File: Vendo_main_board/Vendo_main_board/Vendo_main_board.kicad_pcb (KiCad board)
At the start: 2 copper layers, 60 x 100 mm, 98 parts, among them J1 Screw_Terminal_01x04, J10 Screw_Terminal_01x03, J11 Screw_Terminal_01x02, J12 Screw_Terminal_01x03, J2 Barrel_Jack_MountingPin, J3 Conn_01x05_Pin, J4 Conn_01x05_Pin, J5 BOOT, J6 Screw_Terminal_01x04, J7 FTDI, J9 Conn_01x04_Pin, Q1 Q_NMOS_Depletion_GSD, Q2 Q_NMOS_Depletion_GSD, Q3 Q_NMOS_Depletion_GSD, SW1 SW_Push, SW2 SW_Push, SW3 SW_Push, SW4 SW_Push, SW5 SW_Slide_DPDT, U1 AMS1117-3.3, U2 AP64350SP-13, U3 STM32F103C8T6, U4 PC817, Y1 32.768kHz, Y2 8MHz

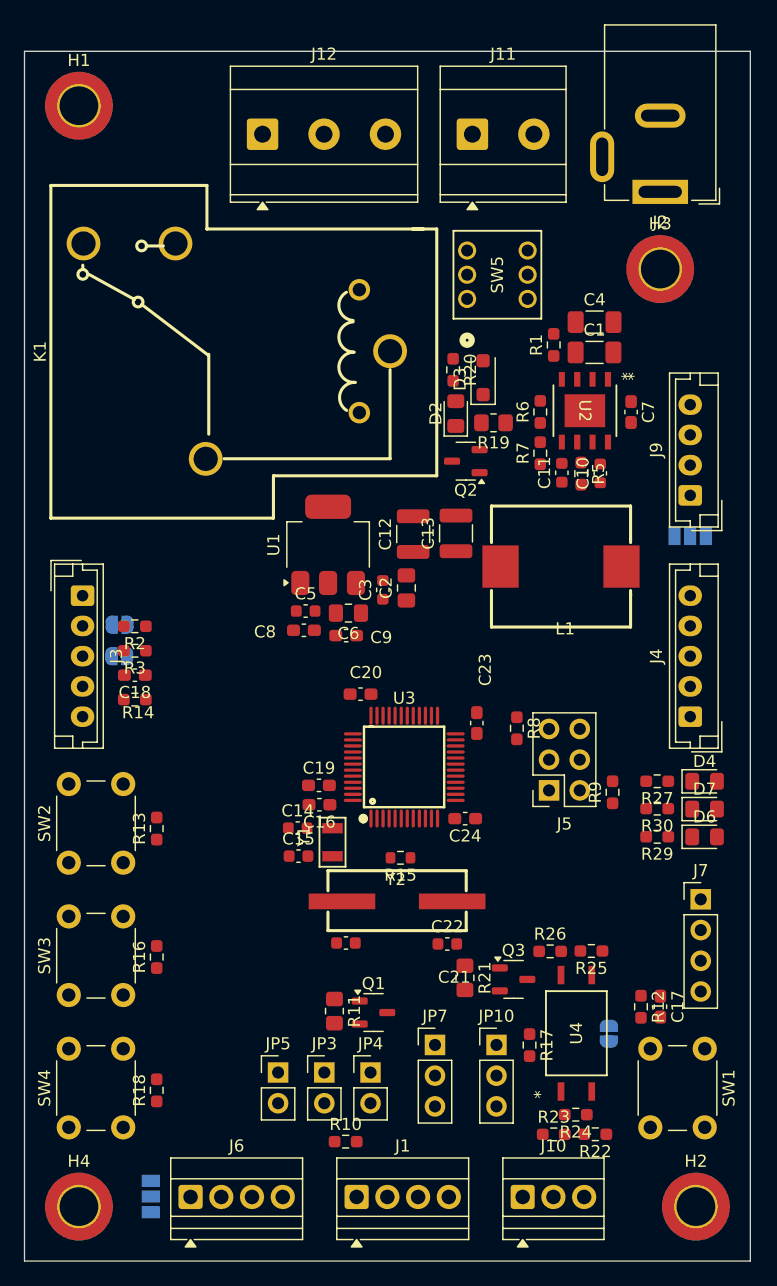
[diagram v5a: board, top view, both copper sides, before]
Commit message: -update schematic and placement
-added buzzer
-finalize pcb placement
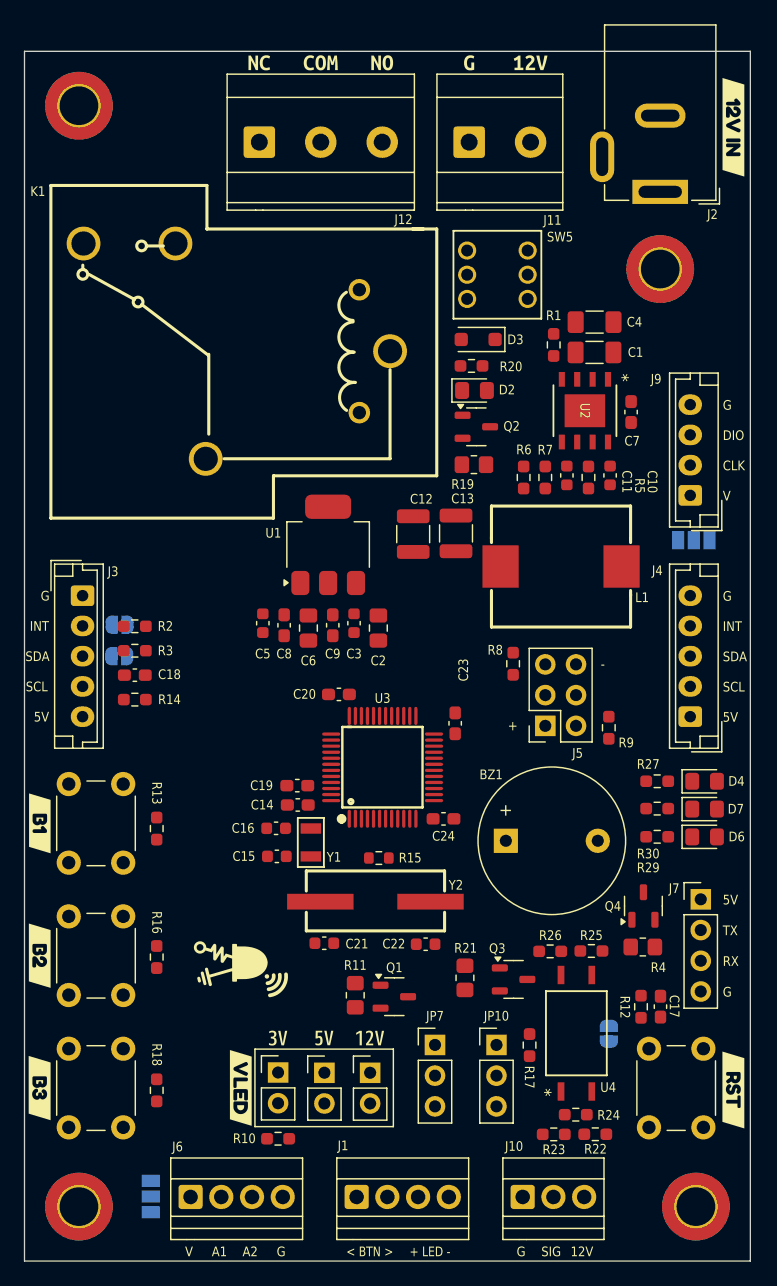
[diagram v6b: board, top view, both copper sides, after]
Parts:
- added BZ1: Buzzer, Buzzer_Beeper:Buzzer_12x9.5RM7.6, F.Cu at (237.9, 92.9)
- added G***: LOGO, InnovKits:innov_logo_5, F.Cu at (216.0, 103.4)
- added G***: LOGO, InnovKits:innov_logo_5, B.Cu at (228.6, 64.7)
- added Q4: Q_NMOS_Depletion_GSD, Package_TO_SOT_SMD:SOT-23-3, F.Cu at (249.3, 98.2)
- added R4: 10K, Resistor_SMD:R_0805_2012Metric_Pad1.20x1.40mm_HandSolder, F.Cu at (249.2, 101.6)
- added kibuzzard-6A0C4EC9: G***, kibuzzard-6A0C4EC9, F.Cu at (234.9, 28.6)
- added kibuzzard-6A0C4ED1: G***, kibuzzard-6A0C4ED1, F.Cu at (227.7, 28.6)
- added kibuzzard-6A0C4EDA: G***, kibuzzard-6A0C4EDA, F.Cu at (222.6, 28.6)
- added kibuzzard-6A0C4EE4: G***, kibuzzard-6A0C4EE4, F.Cu at (217.5, 28.6)
- added kibuzzard-6A0C4FB5: G***, kibuzzard-6A0C4FB5, F.Cu at (239.9, 28.5)
- added kibuzzard-6A0C5003: G***, kibuzzard-6A0C5003, F.Cu at (256.7, 33.9)
- added kibuzzard-6A0C536D: G***, kibuzzard-6A0C536D, F.Cu at (256.7, 113.5)
- added kibuzzard-6A0C57A3: G***, kibuzzard-6A0C57A3, F.Cu at (199.4, 91.4)
- added kibuzzard-6A0C57A8: G***, kibuzzard-6A0C57A8, F.Cu at (199.4, 102.4)
- added kibuzzard-6A0C57AC: G***, kibuzzard-6A0C57AC, F.Cu at (199.3, 113.3)
- added kibuzzard-6A0C5E83: G***, kibuzzard-6A0C5E83, F.Cu at (226.7, 109.2)
- added kibuzzard-6A0C5E89: G***, kibuzzard-6A0C5E89, F.Cu at (222.9, 109.2)
- added kibuzzard-6A0C5E92: G***, kibuzzard-6A0C5E92, F.Cu at (219.1, 109.2)
- added kibuzzard-6A0C5F1E: G***, kibuzzard-6A0C5F1E, F.Cu at (216.0, 113.3)
- moved R10 5.59 mm to (219.1, 117.5)
- moved R6 5.59 mm to (239.4, 62.8), turned to -90 degrees
- moved R8 5.34 mm to (238.5, 78.2)
- moved J5 5.34 mm to (241.2, 83.4)
- moved R9 5.34 mm to (246.4, 83.5)
- moved C2 4.05 mm to (227.3, 75.3)
- moved R19 3.82 mm to (235.2, 61.8)
- moved JP4 3.81 mm to (222.9, 112.0)
- moved JP3 3.79 mm to (226.7, 112.0)
- moved C5 3.68 mm to (217.8, 74.9), turned to 90 degrees
- moved C3 3.64 mm to (225.3, 74.9)
- moved C6 3.53 mm to (221.6, 75.3), turned to 90 degrees
- moved D3 3.18 mm to (235.6, 51.4), turned to 180 degrees
- moved Q2 2.97 mm to (235.4, 58.6), turned to 0 degrees
- moved D2 2.46 mm to (235.3, 55.6), turned to 0 degrees
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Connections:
- J3 pad 1: +5V -> GND
- J3 pad 2: STM_SCL -> I2C_INT
- J3 pad 4: I2C_INT -> STM_SCL
- J3 pad 5: GND -> +5V
- U3 pad 11: unconnected-(U3-PA1-Pad11) -> BUZZER
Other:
- board text added: "+"
- board text added: "+ LED -"
- board text added: "-"
- board text added: "12V"
- board text added: "5V"
- board text added: "< BTN >"
- board text added: "A1"
- board text added: "A2"
- board text added: "CLK"
- board text added: "DESIGNED AND MANUFACTURED BY:"
- board text added: "DIO"
- board text added: "DRIVING INNOVATION FOR LONG TERM SOLUTIONS"
- board text added: "G"
- board text added: "INNOVATION CENTRAL PH"
- board text added: "INT"
- board text added: "RX"
- board text added: "SCL"
- board text added: "SDA"
- board text added: "SIG"
- board text added: "TX"
- board text added: "V"
- board text added: "VENDO BOARD V1.0"

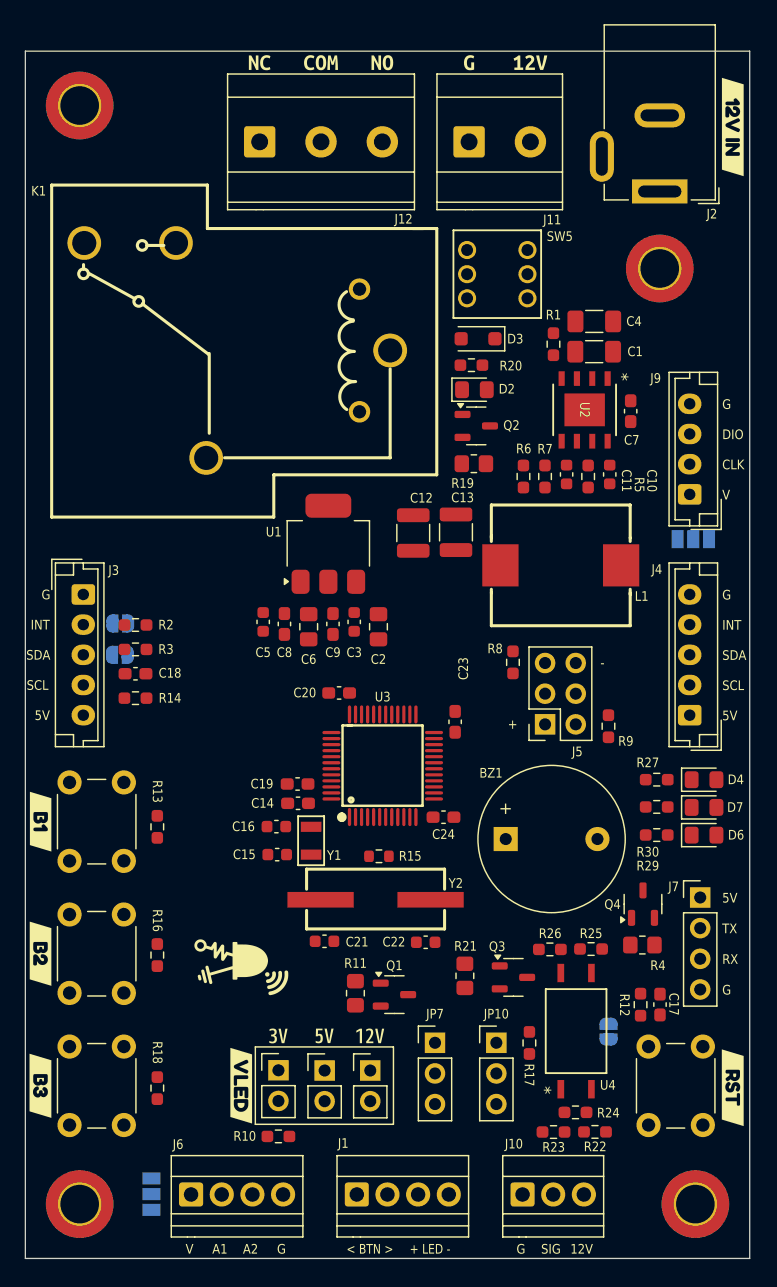
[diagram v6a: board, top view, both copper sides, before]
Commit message: -pcb trace
-pcb trace done
-warnings is due to footprint default silk, and large silk can disregard
-slit will be added
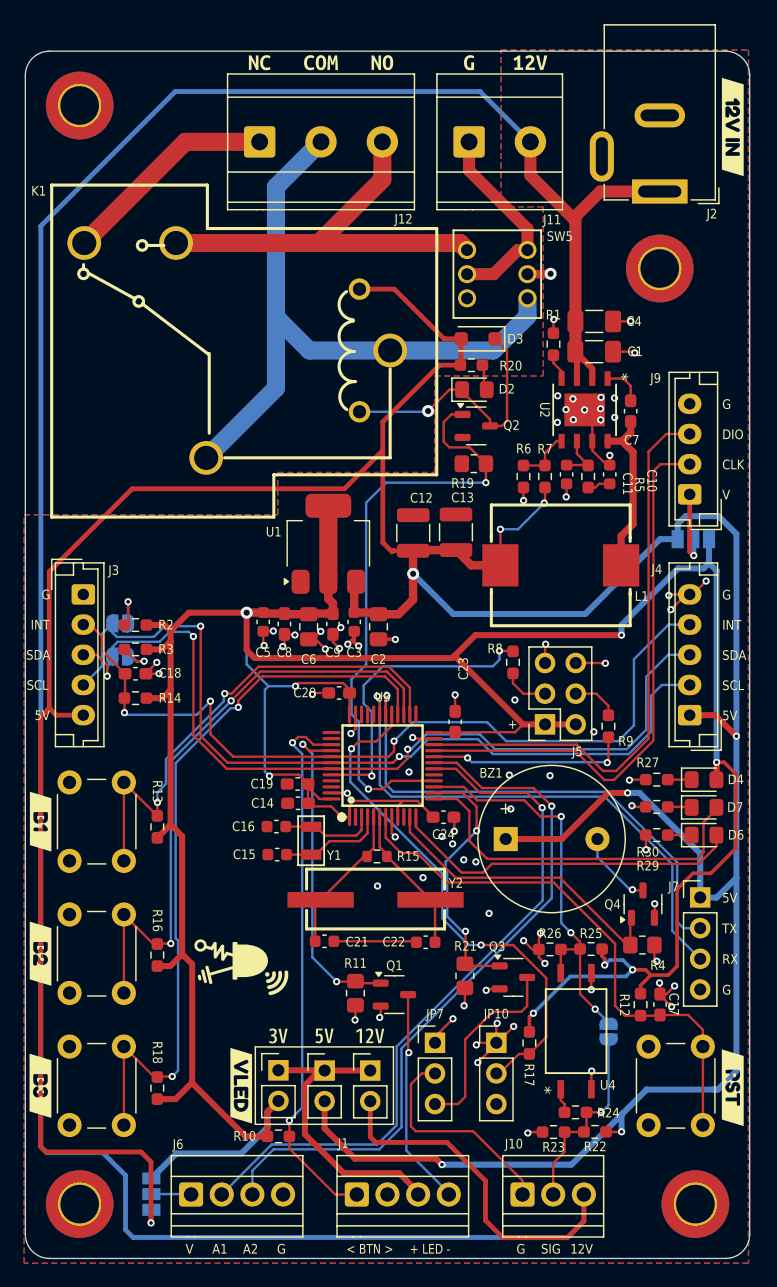
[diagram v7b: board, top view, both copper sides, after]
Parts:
- moved R15 0.16 mm to (227.2, 94.3)
- moved JP2 0.14 mm to (205.9, 77.7)
- turned C11 to -90 degrees
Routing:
- net +5V: track 0.00 -> 313.5 mm, vias 0 -> 8
- net +3.3V: track 0.00 -> 274.6 mm, vias 0 -> 8
- net +12V: track 0.00 -> 237.6 mm
- net GND: track 0.00 -> 84.9 mm, vias 0 -> 79
- net STM_SDA: track 0.00 -> 71.6 mm, vias 0 -> 3
- net STM_SCL: track 0.00 -> 70.6 mm, vias 0 -> 2
- net I2C_INT: track 0.00 -> 69.5 mm, vias 0 -> 3
- net BTN_MODE_3: track 0.00 -> 62.0 mm, vias 0 -> 2
- net AUX_2: track 0.00 -> 58.8 mm, vias 0 -> 1
- net AUX_1: track 0.00 -> 58.5 mm, vias 0 -> 1
- net RLY_COM: track 0.00 -> 54.8 mm
- net BTN_MODE_2: track 0.00 -> 51.6 mm, vias 0 -> 2
- net RLY_DRV: track 0.00 -> 50.4 mm, vias 0 -> 2
- net SEG_DIO: track 0.00 -> 47.6 mm
- net SEG_CLK: track 0.00 -> 46.1 mm
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- added copper zone on B.Cu, net GND
- added copper zone on F.Cu, net GND
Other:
- outline, holes or cut-outs redrawn

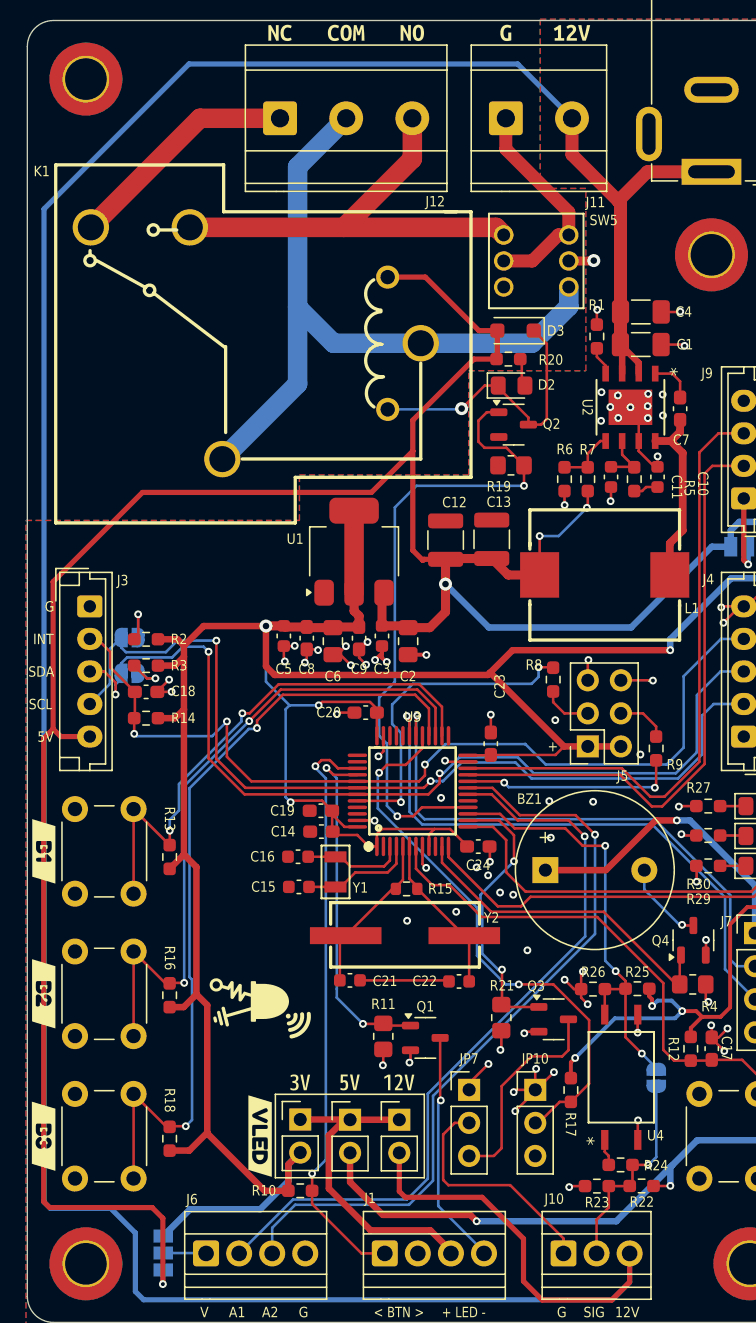
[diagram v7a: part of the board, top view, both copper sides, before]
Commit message: -pcb additional
-added slit for the relay
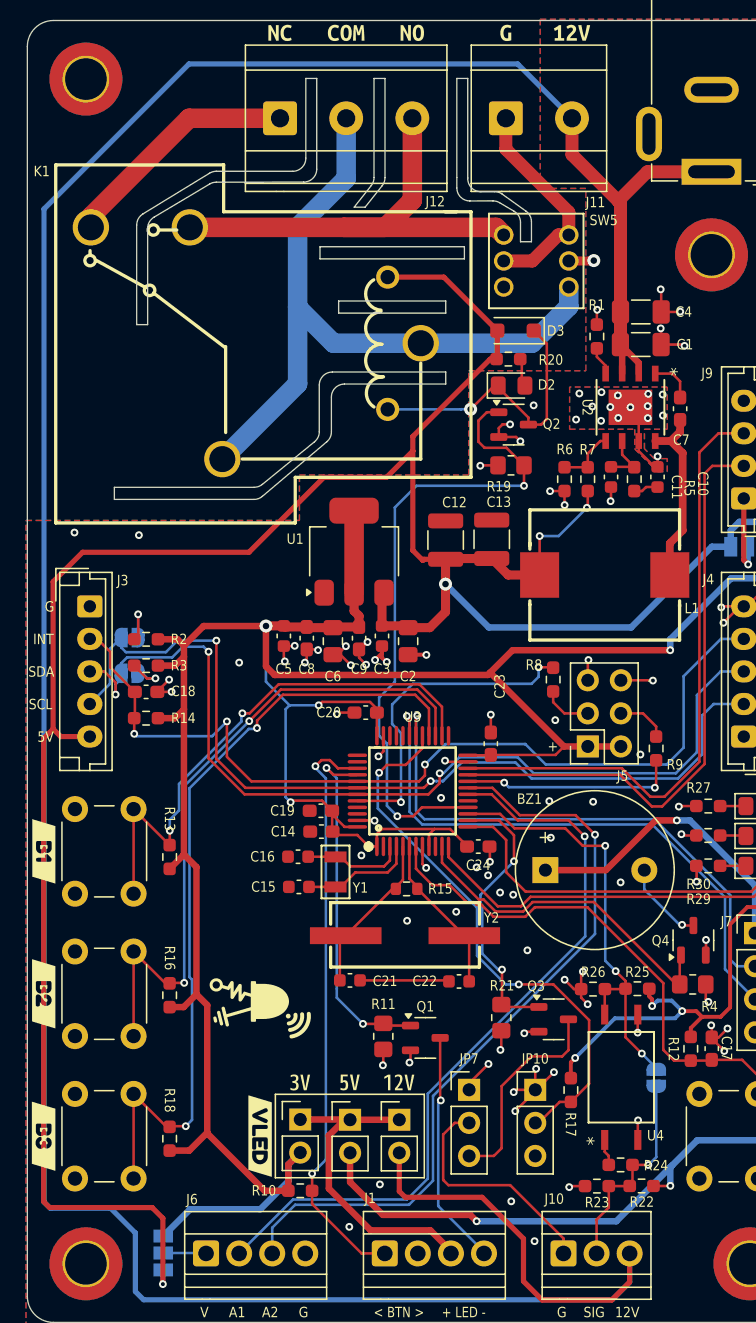
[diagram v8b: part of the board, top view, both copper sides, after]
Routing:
- net GND: track 84.9 -> 93.9 mm, vias 79 -> 98
- net RLY_NO: track 34.9 -> 36.8 mm
- net +5V: track 313.5 -> 312.7 mm
- net STM_RST: track 45.5 -> 46.1 mm
- net BUZZER: track 25.7 -> 26.3 mm
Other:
- outline, holes or cut-outs redrawn
